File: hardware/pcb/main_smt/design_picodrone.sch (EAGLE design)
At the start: 2 parts, among them U1 STM32F103C8T6, U2 MPU-6050

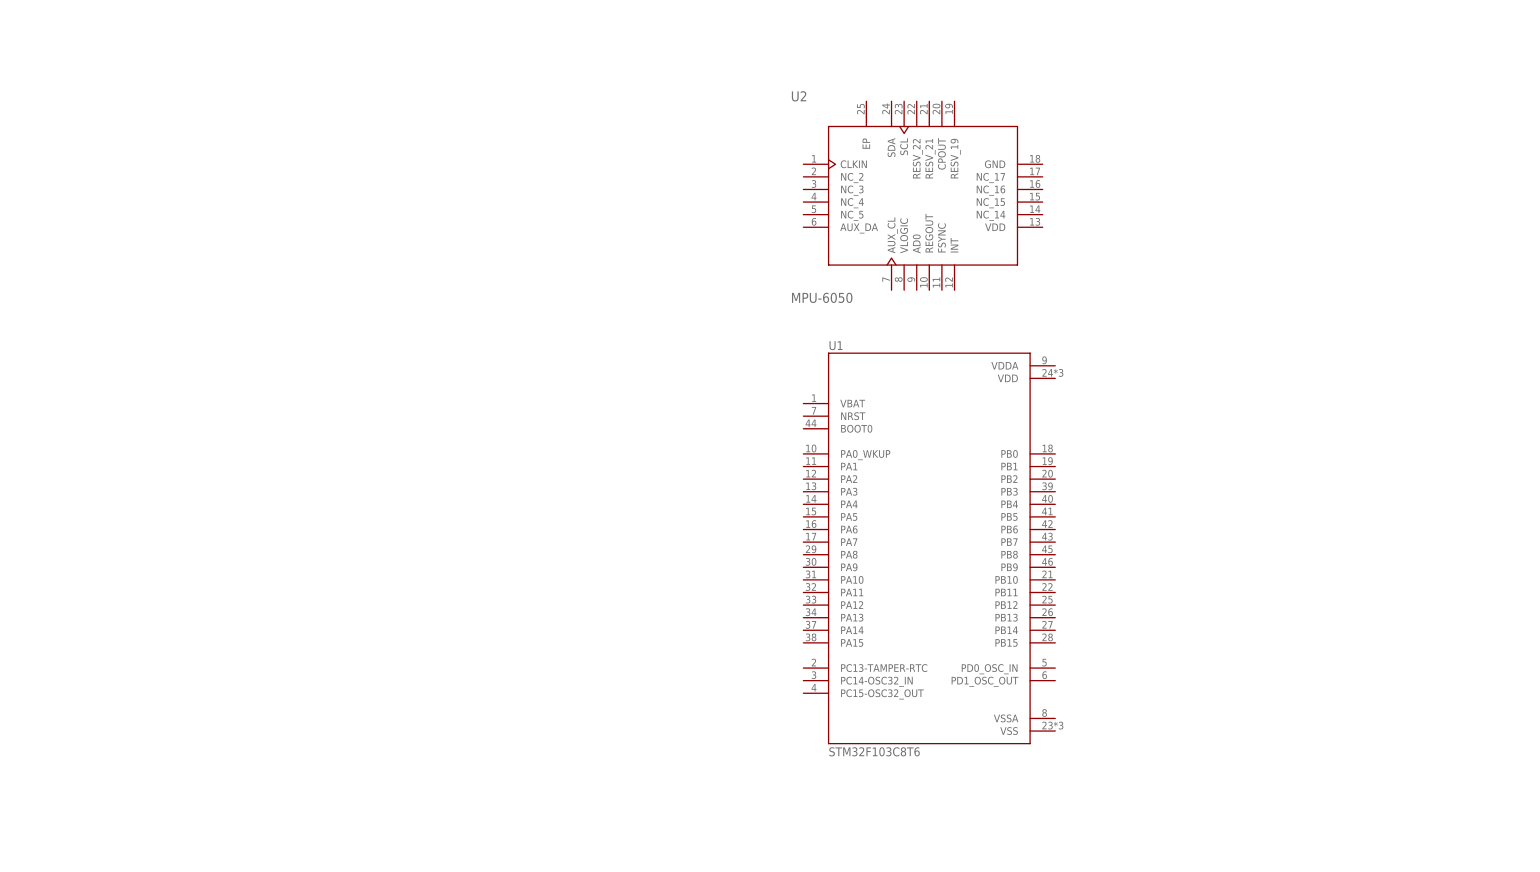
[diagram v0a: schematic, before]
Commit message: completed mosfet test pcb used for testing V, I characteristics of different sot23 fets
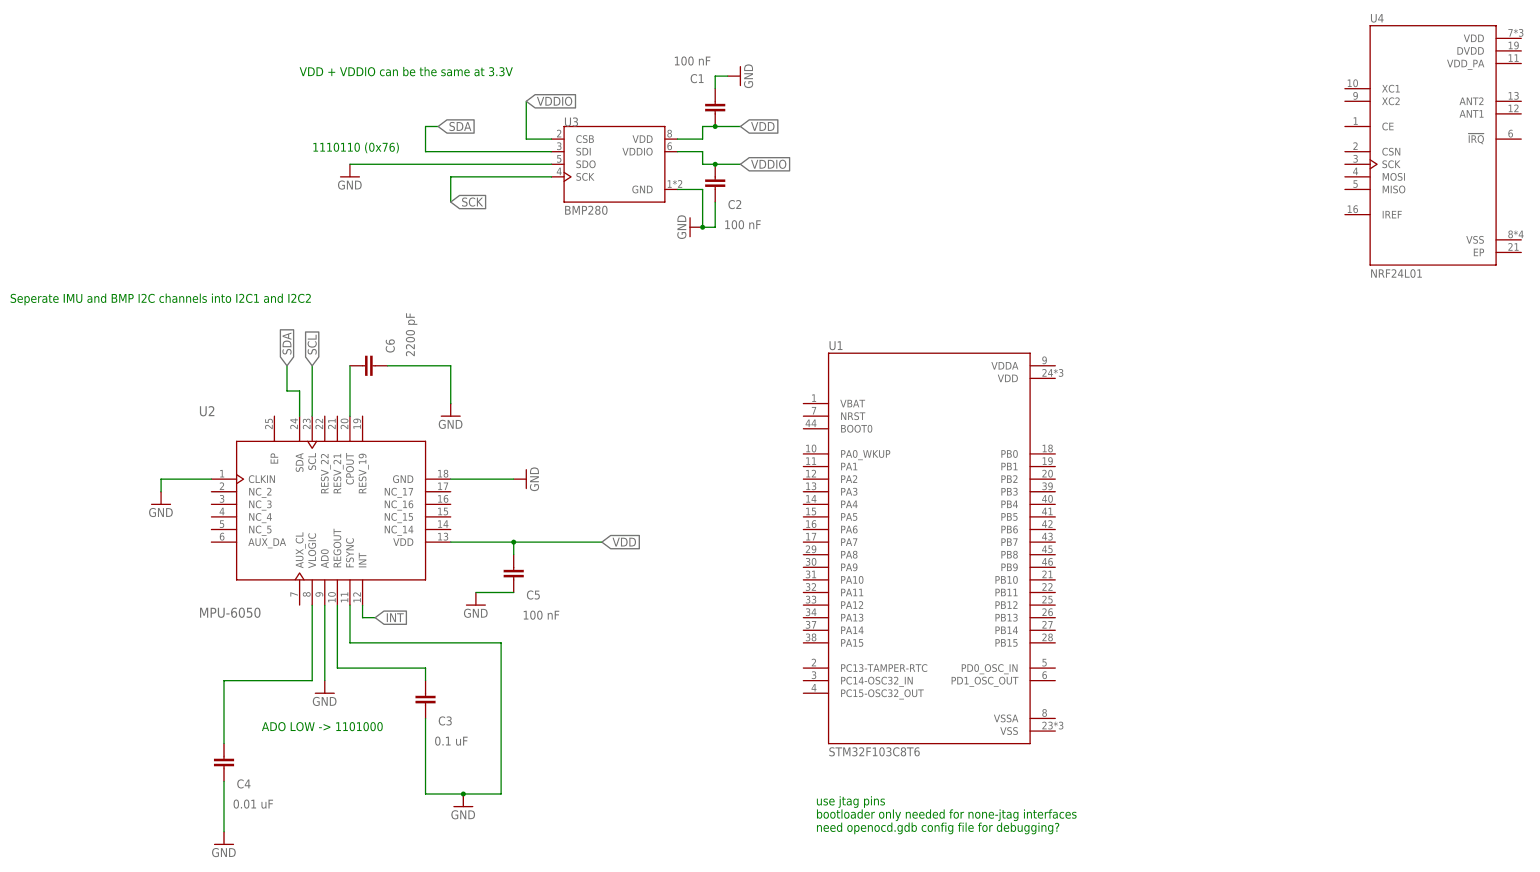
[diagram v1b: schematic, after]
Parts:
- added C1, C2, C5: 100 nF, Resistor_Capacitor:C0603C100C5GACTU
- added C3: 0.1 uF, Resistor_Capacitor:C0603C100C5GACTU
- added C4: 0.01 uF, Resistor_Capacitor:C0603C100C5GACTU
- added C6: 2200 pF, Resistor_Capacitor:C0603C100C5GACTU
- added U3: BMP280, BMP280:BMP280
- added U4: NRF24L01, NRF24L01:NRF24L01
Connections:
- new net GND: C1.1, C2.2, C3.2, C4.2, C5.2, C6.2, U2.AD0, U2.CLKIN, U2.FSYNC, U2.GND, U3.GND, U3.SDO
- new net INT: U2.INT
- new net N$1: C4.1, U2.VLOGIC
- new net N$2: C3.1, U2.REGOUT
- new net N$3: C6.1, U2.CPOUT
- new net SCK: U3.SCK
- new net SCL: U2.SCL
- new net SDA: U2.SDA, U3.SDI
- new net VDD: C1.2, C5.1, U2.VDD, U3.VDD
- new net VDDIO: C2.1, U3.CSB, U3.VDDIO
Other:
- note added: "1110110 (0x76)"
- note added: "ADO LOW -> 1101000"
- note added: "Seperate IMU and BMP I2C channels into I2C1 and I2C2"
- note added: "VDD + VDDIO can be the same at 3.3V"
- note added: "use jtag pins bootloader only needed for none-jtag interfaces need openocd.gdb config file for debugging?"
- moved on the sheet: U2
